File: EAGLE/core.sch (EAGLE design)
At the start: 46 parts, among them IC1 MCP1825S-3302E, Q1 MMDT3904, U3 STM32F10XCXT6, U4 SST25VF040B-S2, X1 USB-MICROB, X2 IPEX-20279-001E, Y1 8Mhz, Y2 32Khz

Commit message: Updated Schematic - Added Tantalum Cap for VDDA and Rearranged RGB Wiring
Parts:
- added C17: 10uF, Spark:TANT-CAP0603
- C2: value 1uF -> 4.7uF
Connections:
- removed net N$18: LED_RGB.CRED, RN1C.1
- new net N$10: LED_RGB.CRED, RN1A.1
- net D7: now also RN1D.2; no longer RN1D.1
- net GND: now also C17.-
- net LED1: now also RN1D.1; no longer RN1D.2
- net LED2: now also RN1A.2; no longer RN1C.2
- net LED4: now also RN1C.2; no longer RN1A.2
- net N$14: now also RN1C.1; no longer RN1A.1
- net VDDA: now also C17.+
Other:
- moved on the sheet: C13, LED_RGB, LED_USR

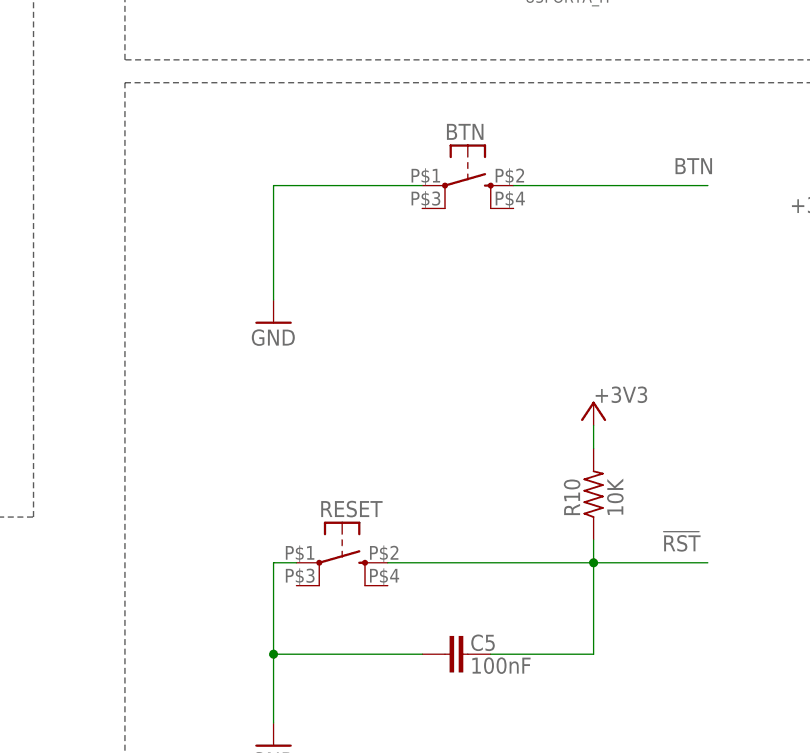
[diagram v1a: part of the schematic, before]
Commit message: Tactile switch replaced in Schematic and Layout
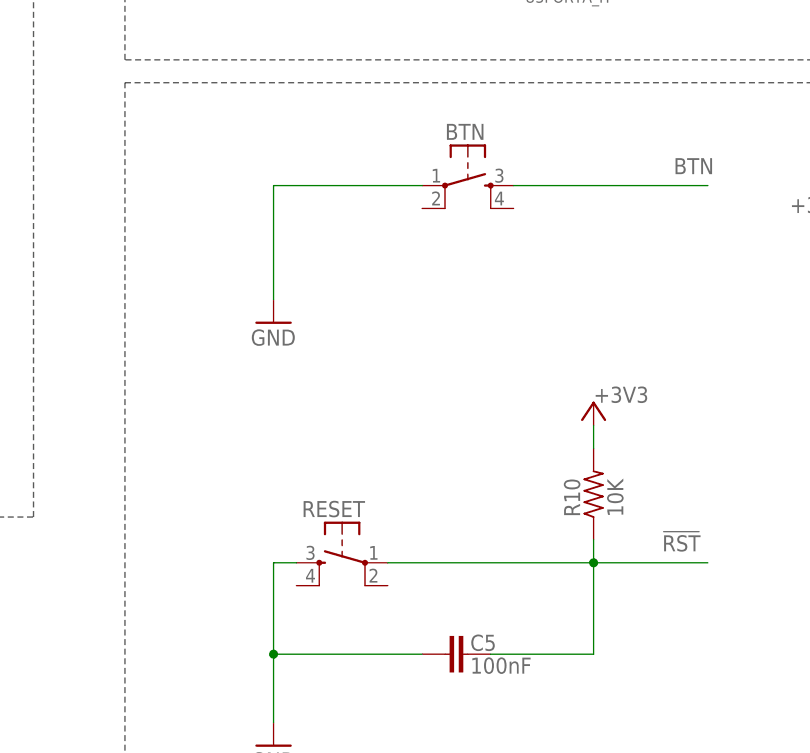
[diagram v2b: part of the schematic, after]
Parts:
- BTN, RESET: device okie:BUTTON-KMR241GLFS -> Spark:TAC_SWITCHSMD
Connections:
- net !RST: now also RESET.1; no longer RESET.2
- net BTN: now also BTN.3; no longer BTN.2
- net GND: now also RESET.3; no longer RESET.1
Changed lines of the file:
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@@
 <part name="GND11" library="supply1" deviceset="GND" device=""/>
 <part name="C3" library="rcl" deviceset="C-EU" device="C0603" value="100nF"/>
-<part name="RESET" library="okie" deviceset="BUTTON-KMR241GLFS" device="" value="KMR211GLFS"/>
+<part name="RESET" library="Spark" deviceset="TAC_SWITCH" device="SMD" value="KMR211GLFS"/>
 <part name="R10" library="rcl" deviceset="R-US_" device="R0603" value="10K"/>
-<part name="BTN" library="okie" deviceset="BUTTON-KMR241GLFS" device="" value="KMR211GLFS"/>
+<part name="BTN" library="Spark" deviceset="TAC_SWITCH" device="SMD" value="KMR211GLFS"/>
 <part name="GND1" library="SparkFun" deviceset="GND" device=""/>
 <part name="LED_USR" library="SparkFun" deviceset="LED" device="0603"/>
@@
 </instance>
 <instance part="U3" gate="RESET" x="436.88" y="170.18"/>
-<instance part="RESET" gate="G$1" x="280.67" y="33.02" smashed="yes">
-<attribute name="NAME" x="278.13" y="38.1" size="1.778" layer="95"/>
+<instance part="RESET" gate="S" x="280.67" y="33.02" smashed="yes" rot="MR0">
+<attribute name="NAME" x="283.21" y="38.1" size="1.778" layer="95" rot="MR0"/>
 </instance>
 <instance part="R10" gate="G$1" x="308.61" y="40.64" smashed="yes" rot="R90">
@@
 <attribute name="VALUE" x="311.912" y="38.1" size="1.778" layer="96" rot="R90"/>
 </instance>
-<instance part="BTN" gate="G$1" x="294.64" y="74.93" smashed="yes">
+<instance part="BTN" gate="S" x="294.64" y="74.93" smashed="yes">
 <attribute name="NAME" x="292.1" y="80.01" size="1.778" layer="95"/>
 </instance>
@@
 <pinref part="GND13" gate="1" pin="GND"/>
 <wire x1="273.05" y1="74.93" x2="273.05" y2="62.23" width="0.1524" layer="91"/>
-<pinref part="BTN" gate="G$1" pin="1"/>
+<pinref part="BTN" gate="S" pin="1"/>
 <wire x1="289.56" y1="74.93" x2="273.05" y2="74.93" width="0.1524" layer="91"/>
 </segment>
@@
 </segment>
 <segment>
+<pinref part="C5" gate="G$1" pin="1"/>
+<wire x1="289.56" y1="22.86" x2="273.05" y2="22.86" width="0.1524" layer="91"/>
+<pinref part="GND12" gate="1" pin="GND"/>
+<wire x1="273.05" y1="22.86" x2="273.05" y2="15.24" width="0.1524" layer="91"/>
+<pinref part="RESET" gate="S" pin="3"/>
 <wire x1="275.59" y1="33.02" x2="273.05" y2="33.02" width="0.1524" layer="91"/>
 <wire x1="273.05" y1="33.02" x2="273.05" y2="22.86" width="0.1524" layer="91"/>
-<pinref part="RESET" gate="G$1" pin="1"/>
-<pinref part="C5" gate="G$1" pin="1"/>
-<wire x1="289.56" y1="22.86" x2="273.05" y2="22.86" width="0.1524" layer="91"/>
 <junction x="273.05" y="22.86"/>
-<pinref part="GND12" gate="1" pin="GND"/>
-<wire x1="273.05" y1="22.86" x2="273.05" y2="15.24" width="0.1524" layer="91"/>
 </segment>
 <segment>
@@
 </segment>
 <segment>
-<wire x1="285.75" y1="33.02" x2="308.61" y2="33.02" width="0.1524" layer="91"/>
 <wire x1="308.61" y1="33.02" x2="308.61" y2="35.56" width="0.1524" layer="91"/>
 <label x="316.23" y="34.29" size="1.778" layer="95"/>
-<pinref part="RESET" gate="G$1" pin="2"/>
 <pinref part="R10" gate="G$1" pin="1"/>
 <pinref part="C5" gate="G$1" pin="2"/>
@@
 <junction x="308.61" y="33.02"/>
 <wire x1="308.61" y1="33.02" x2="321.31" y2="33.02" width="0.1524" layer="91"/>
+<pinref part="RESET" gate="S" pin="1"/>
+<wire x1="285.75" y1="33.02" x2="308.61" y2="33.02" width="0.1524" layer="91"/>
 </segment>
 <segment>
@@
 <net name="BTN" class="0">
 <segment>
-<pinref part="BTN" gate="G$1" pin="2"/>
+<pinref part="BTN" gate="S" pin="3"/>
 <wire x1="299.72" y1="74.93" x2="321.31" y2="74.93" width="0.1524" layer="91"/>
 <label x="317.5" y="76.2" size="1.778" layer="95"/>

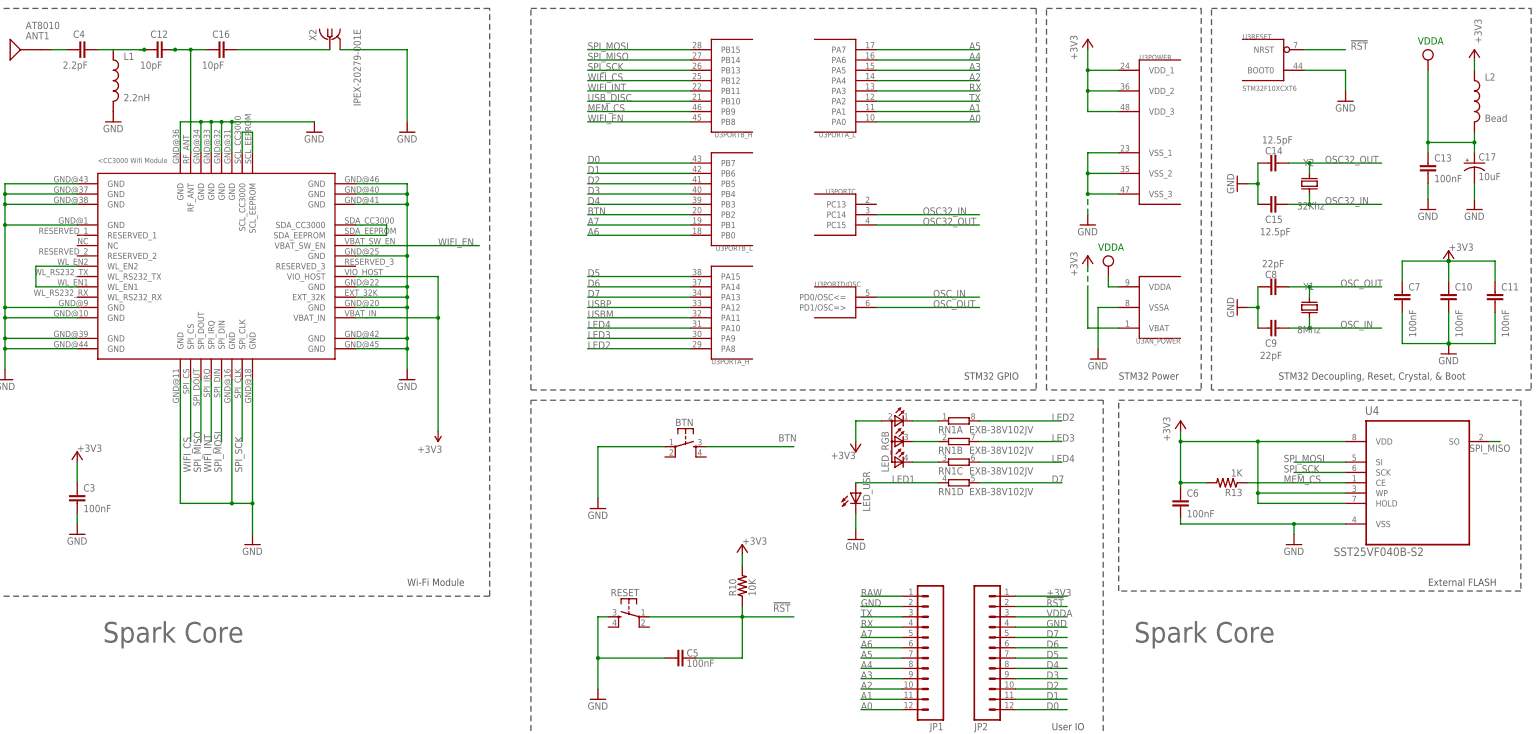
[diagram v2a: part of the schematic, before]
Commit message: Renumbered components
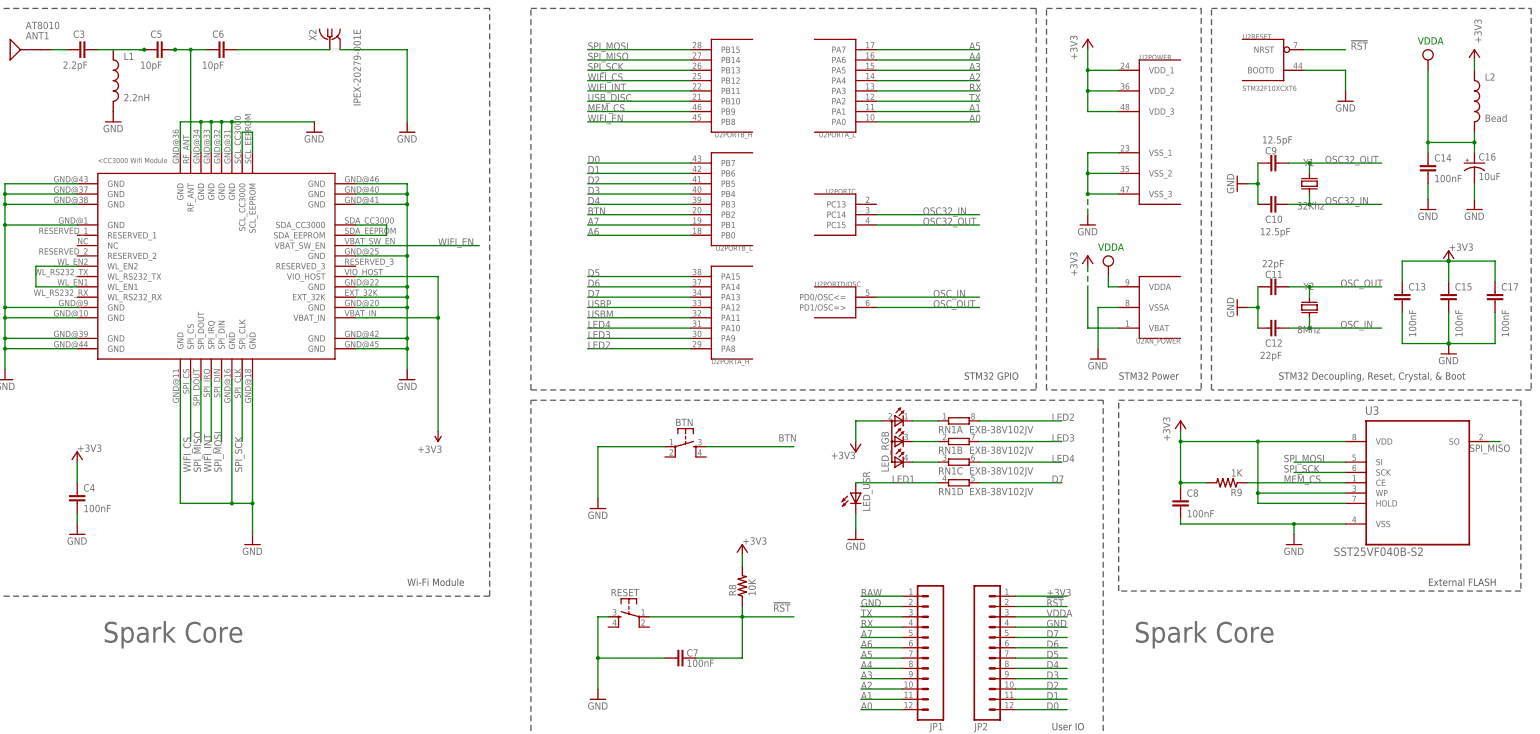
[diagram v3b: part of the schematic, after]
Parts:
- removed U4: SST25VF040B-S2, Spark:SST25VF040B-S2
- added U1: (no value), CC3000:CC3000
- C10: value 100nF -> 12.5pF
- C11: value 100nF -> 22pF
- C12: value 10pF -> 22pF
- C14, C15: value 12.5pF -> 100nF
- C16: value 10pF -> 10uF; device rcl:C-EUC0603 -> Spark:TANT-CAP0603
- C17: value 10uF -> 100nF; device Spark:TANT-CAP0603 -> rcl:C-EUC0603
- C3: value 100nF -> 2.2pF
- C4: value 2.2pF -> 100nF
- C5, C6: value 100nF -> 10pF
- C8: value 22pF -> 100nF
- C9: value 22pF -> 12.5pF
- U2: value (none) -> STM32F10XCXT6; device CC3000:CC3000 -> stm32:STM32F10XCXT6
- U3: value STM32F10XCXT6 -> SST25VF040B-S2; device stm32:STM32F10XCXT6 -> Spark:SST25VF040B-S2
- Y1: value 8Mhz -> 32Khz; device Spark:Q_3.2X2.5 -> Spark:Q_FC135
- Y2: value 32Khz -> 8Mhz; device Spark:Q_FC135 -> Spark:Q_3.2X2.5
- renumbered R10 to R8, R13 to R9
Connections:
- net !RST: now also C7.2, U2RESET.NRST; no longer C5.2, U3RESET.NRST
- net +3V3: now also C13.1, C15.1, C17.1, C4.1, C8.1, U1.VBAT_IN, U1.VIO_HOST, U2AN_POWER.VBAT, U2POWER.VDD_1, U2POWER.VDD_2, U2POWER.VDD_3, U3.HOLD, U3.VDD, U3.WP; no longer C10.1, C11.1, C3.1, C6.1, C7.1, U2.VBAT_IN, U2.VIO_HOST, U3AN_POWER.VBAT, U3POWER.VDD_1, U3POWER.VDD_2, U3POWER.VDD_3, U4.HOLD, U4.VDD, U4.WP
- net A0: now also U2PORTA_L.PA0; no longer U3PORTA_L.PA0
- net A1: now also U2PORTA_L.PA1; no longer U3PORTA_L.PA1
- net A2: now also U2PORTA_L.PA4; no longer U3PORTA_L.PA4
- net A3: now also U2PORTA_L.PA5; no longer U3PORTA_L.PA5
- net A4: now also U2PORTA_L.PA6; no longer U3PORTA_L.PA6
- net A5: now also U2PORTA_L.PA7; no longer U3PORTA_L.PA7
- net A6: now also U2PORTB_L.PB0; no longer U3PORTB_L.PB0
- net A7: now also U2PORTB_L.PB1; no longer U3PORTB_L.PB1
- net BTN: now also U2PORTB_L.PB2; no longer U3PORTB_L.PB2
- net D0: now also U2PORTB_L.PB7; no longer U3PORTB_L.PB7
- net D1: now also U2PORTB_L.PB6; no longer U3PORTB_L.PB6
- net D2: now also U2PORTB_L.PB5; no longer U3PORTB_L.PB5
- net D3: now also U2PORTB_L.PB4; no longer U3PORTB_L.PB4
- net D4: now also U2PORTB_L.PB3; no longer U3PORTB_L.PB3
- net D5: now also U2PORTA_H.PA15; no longer U3PORTA_H.PA15
- net D6: now also U2PORTA_H.PA14; no longer U3PORTA_H.PA14
- net D7: now also U2PORTA_H.PA13; no longer U3PORTA_H.PA13
- net GND: now also C12.2, C16.-, C17.2, C4.2, C7.1, U1.EXT_32K, U1.GND@1, U1.GND@10, U1.GND@11, U1.GND@16, U1.GND@18, U1.GND@20, U1.GND@22, U1.GND@25, U1.GND@31, U1.GND@32, U1.GND@33, U1.GND@34, U1.GND@36, U1.GND@37, U1.GND@38, U1.GND@39, U1.GND@40, U1.GND@41, U1.GND@42, U1.GND@43, U1.GND@44, U1.GND@45, U1.GND@46, U1.GND@9, U2AN_POWER.VSSA, U2POWER.VSS_1, U2POWER.VSS_2, U2POWER.VSS_3, U2RESET.BOOT0, U3.VSS; no longer C17.-, C3.2, C5.1, C6.2, C7.2, U2.EXT_32K, U2.GND@1, U2.GND@10, U2.GND@11, U2.GND@16, U2.GND@18, U2.GND@20, U2.GND@22, U2.GND@25, U2.GND@31, U2.GND@32, U2.GND@33, U2.GND@34, U2.GND@36, U2.GND@37, U2.GND@38, U2.GND@39, U2.GND@40, U2.GND@41, U2.GND@42, U2.GND@43, U2.GND@44, U2.GND@45, U2.GND@46, U2.GND@9, U3AN_POWER.VSSA, U3POWER.VSS_1, U3POWER.VSS_2, U3POWER.VSS_3, U3RESET.BOOT0, U4.VSS
- net LED2: now also U2PORTA_H.PA8; no longer U3PORTA_H.PA8
- net LED3: now also U2PORTA_H.PA9; no longer U3PORTA_H.PA9
- net LED4: now also U2PORTA_H.PA10; no longer U3PORTA_H.PA10
- net MEM_CS: now also U2PORTB_H.PB9, U3.CE; no longer U3PORTB_H.PB9, U4.CE
- net N$15: now also U1.SDA_CC3000, U1.SDA_EEPROM; no longer U2.SDA_CC3000, U2.SDA_EEPROM
- net N$2: now also C6.2; no longer C16.2
- net N$3: now also C3.1; no longer C4.1
- net N$4: now also C5.2, C6.1, U1.RF_ANT; no longer C12.2, C16.1, U2.RF_ANT
- net N$5: now also C3.2, C5.1; no longer C12.1, C4.2
- net N$7: now also U1.SCL_CC3000, U1.SCL_EEPROM; no longer U2.SCL_CC3000, U2.SCL_EEPROM
- net N$9: now also U1.WL_EN1, U1.WL_EN2; no longer U2.WL_EN1, U2.WL_EN2
- net OSC32_IN: now also C10.1, U2PORTC.PC14, Y1.1; no longer C15.1, U3PORTC.PC14, Y2.1
- net OSC32_OUT: now also C9.1, U2PORTC.PC15, Y1.2; no longer C14.1, U3PORTC.PC15, Y2.2
- net OSC_IN: now also C12.1, U2PORTD/OSC.PD0/OSC<=, Y2.1; no longer C9.1, U3PORTD/OSC.PD0/OSC<=, Y1.1
- net OSC_OUT: now also C11.1, U2PORTD/OSC.PD1/OSC=>, Y2.2; no longer C8.1, U3PORTD/OSC.PD1/OSC=>, Y1.2
- net RX: now also U2PORTA_L.PA3; no longer U3PORTA_L.PA3
- net SPI_MISO: now also U1.SPI_DOUT, U2PORTB_H.PB14, U3.SO; no longer U2.SPI_DOUT, U3PORTB_H.PB14, U4.SO
- net SPI_MOSI: now also U1.SPI_DIN, U2PORTB_H.PB15, U3.SI; no longer U2.SPI_DIN, U3PORTB_H.PB15, U4.SI
- net SPI_SCK: now also U1.SPI_CLK, U2PORTB_H.PB13, U3.SCK; no longer U2.SPI_CLK, U3PORTB_H.PB13, U4.SCK
- net TX: now also U2PORTA_L.PA2; no longer U3PORTA_L.PA2
- net USBM: now also U2PORTA_H.PA11; no longer U3PORTA_H.PA11
- net USBP: now also U2PORTA_H.PA12; no longer U3PORTA_H.PA12
- net USB_DISC: now also U2PORTB_H.PB10; no longer U3PORTB_H.PB10
- net VDDA: now also C14.1, C16.+, U2AN_POWER.VDDA; no longer C13.1, C17.+, U3AN_POWER.VDDA
- net WIFI_CS: now also U1.SPI_CS, U2PORTB_H.PB12; no longer U2.SPI_CS, U3PORTB_H.PB12
- net WIFI_EN: now also U1.VBAT_SW_EN, U2PORTB_H.PB8; no longer U2.VBAT_SW_EN, U3PORTB_H.PB8
- net WIFI_INT: now also U1.SPI_IRQ, U2PORTB_H.PB11; no longer U2.SPI_IRQ, U3PORTB_H.PB11
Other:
- moved on the sheet: C10, C11, C12, C13, C14, C15, C3, C4, C5, C6, C7, C8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

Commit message: Replaced C16 - Tantalum 0603 with Tantalum 1206
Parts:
- C16: device Spark:TANT-CAP0603 -> Spark:TANT-CAP1206
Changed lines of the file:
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@@
 <part name="ANT1" library="Spark" deviceset="AT8010" device=""/>
 <part name="C5" library="rcl" deviceset="C-EU" device="C0603" value="10pF"/>
-<part name="C16" library="Spark" deviceset="TANT-CAP" device="0603" value="10uF"/>
+<part name="C16" library="Spark" deviceset="TANT-CAP" device="1206" value="10uF"/>
 <part name="GND14" library="supply1" deviceset="GND" device=""/>
 </parts>
